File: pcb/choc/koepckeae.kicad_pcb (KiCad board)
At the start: 2 copper layers, 239.8 x 115.1 mm, 49 parts, among them J1 Conn_01x09_Socket, J2 Conn_01x02_Socket, J3 Conn_01x02_Socket, K1 PG1350, K10 PG1350, K11 PG1350, K12 PG1350, K13 PG1350, K14 PG1350, K15 PG1350, K16 PG1350, K17 PG1350, K18 PG1350, K19 PG1350, K2 PG1350, K20 PG1350, K21 PG1350, K22 PG1350, K23 PG1350, K24 PG1350, K25 PG1350, K26 PG1350, K27 PG1350, K28 PG1350, K29 PG1350, K3 PG1350, K30 PG1350, K31 PG1350, K32 PG1350, K33 PG1350, K34 PG1350, K4 PG1350, K5 PG1350, K6 PG1350, K7 PG1350, K8 PG1350, K9 PG1350, SW1 SW_Push, SW2 SW_SPDT, U1 Seeeduino Xiao nRF52840, U2 74HC595

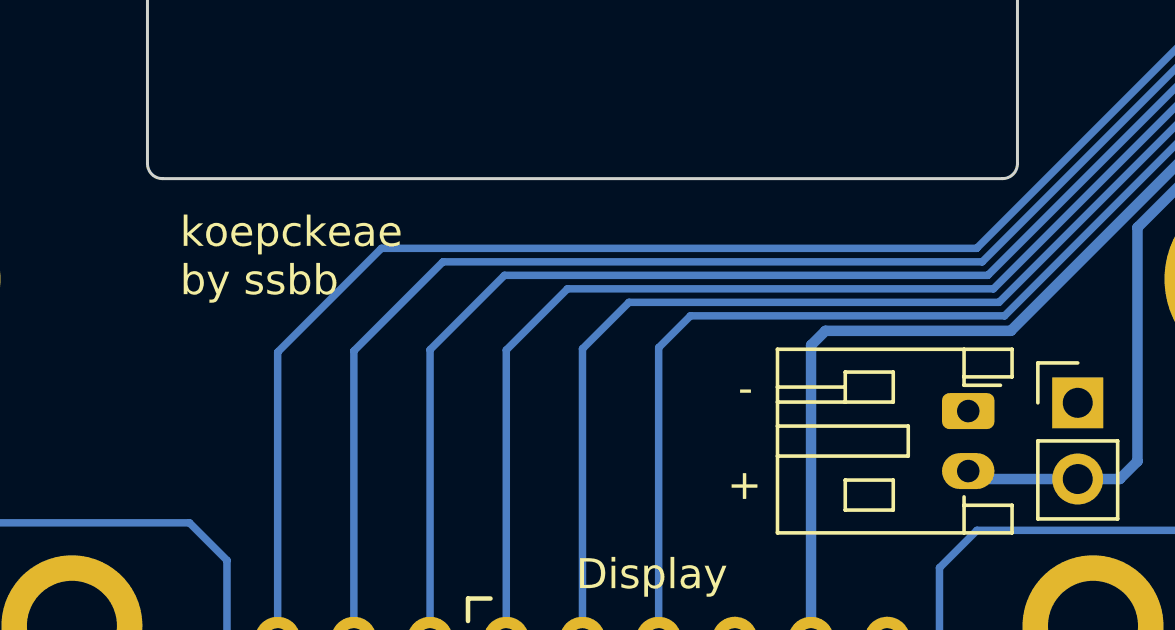
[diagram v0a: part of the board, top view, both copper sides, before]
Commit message: Change fsilk label
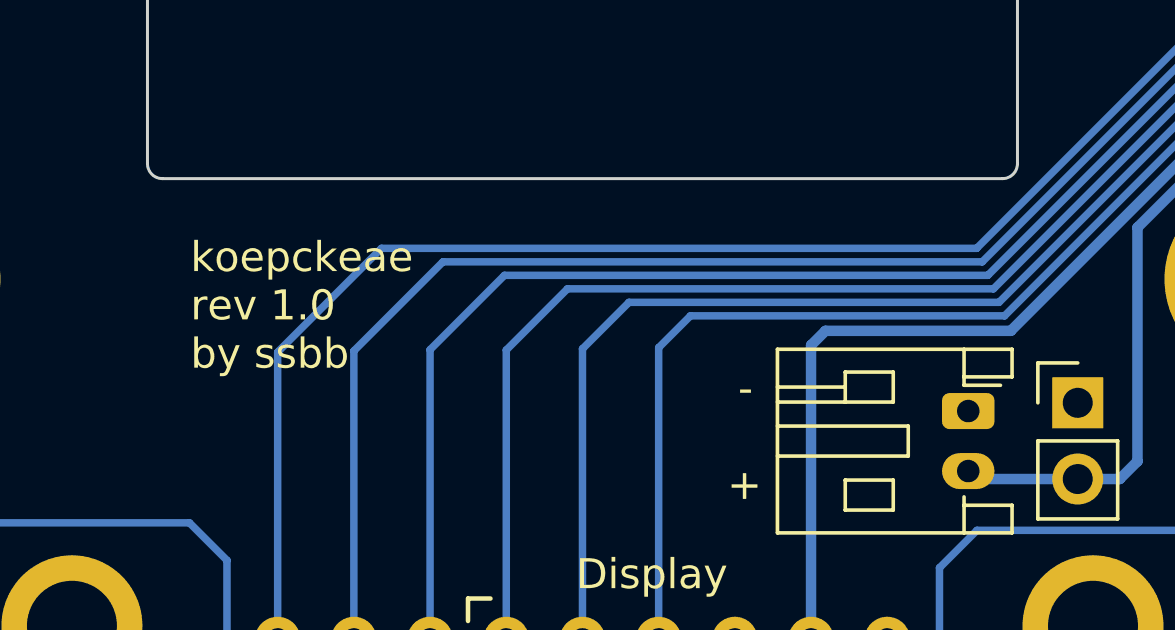
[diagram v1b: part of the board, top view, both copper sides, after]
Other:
- board text added: "koepckeae rev 1.0 by ssbb"
- board text removed: "koepckeae by ssbb"
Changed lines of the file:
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@@
     (fp_line (start 3.95 6.25) (end 3.95 -1.35)
       (stroke (width 0.1) (type solid)) (layer "F.Fab"))
-    (pad "1" thru_hole roundrect (at 0 0 270) (size 1.2 1.75) (drill 0.75) (layers "*.Cu" "*.Mask") (roundrect_rratio 0.208333)
+    (pad "1" thru_hole roundrect (at 0 0 270) (size 1.2 1.75) (drill 0.75) (layers "*.Cu" "*.Mask") (roundrect_rratio 0.2083333333)
       (net 7 "GND") (pinfunction "Pin_1") (pintype "passive"))
     (pad "2" thru_hole oval (at 2 0 270) (size 1.2 1.75) (drill 0.75) (layers "*.Cu" "*.Mask")
@@
   (gr_arc (start 92.682172 34.649118) (mid 94.092906 33.356465) (end 96.004485 33.439898)
     (stroke (width 0.1) (type default)) (layer "Edge.Cuts"))
-  (gr_text "koepckeae \nby ssbb\n" (at 136.304495 125.8) (layer "F.SilkS")
+  (gr_text "koepckeae \nrev 1.0\nby ssbb" (at 136.654495 128.25) (layer "F.SilkS")
     (effects (font (size 1 1) (thickness 0.15)) (justify left bottom))
   )
